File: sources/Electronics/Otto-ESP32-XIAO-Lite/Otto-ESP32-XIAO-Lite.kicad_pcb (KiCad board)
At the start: 2 copper layers, 60 x 52 mm, 54 parts, among them J1 Conn_01x03, J10 Conn_01x02, J12 OLED 0,91" - I2C (SKU21796), J13 MPU6050, J2 Conn_01x03, J3 Conn_01x03, J4 Conn_01x03, J5 Conn_01x03, J6 Conn_01x03, J7 Conn_01x04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

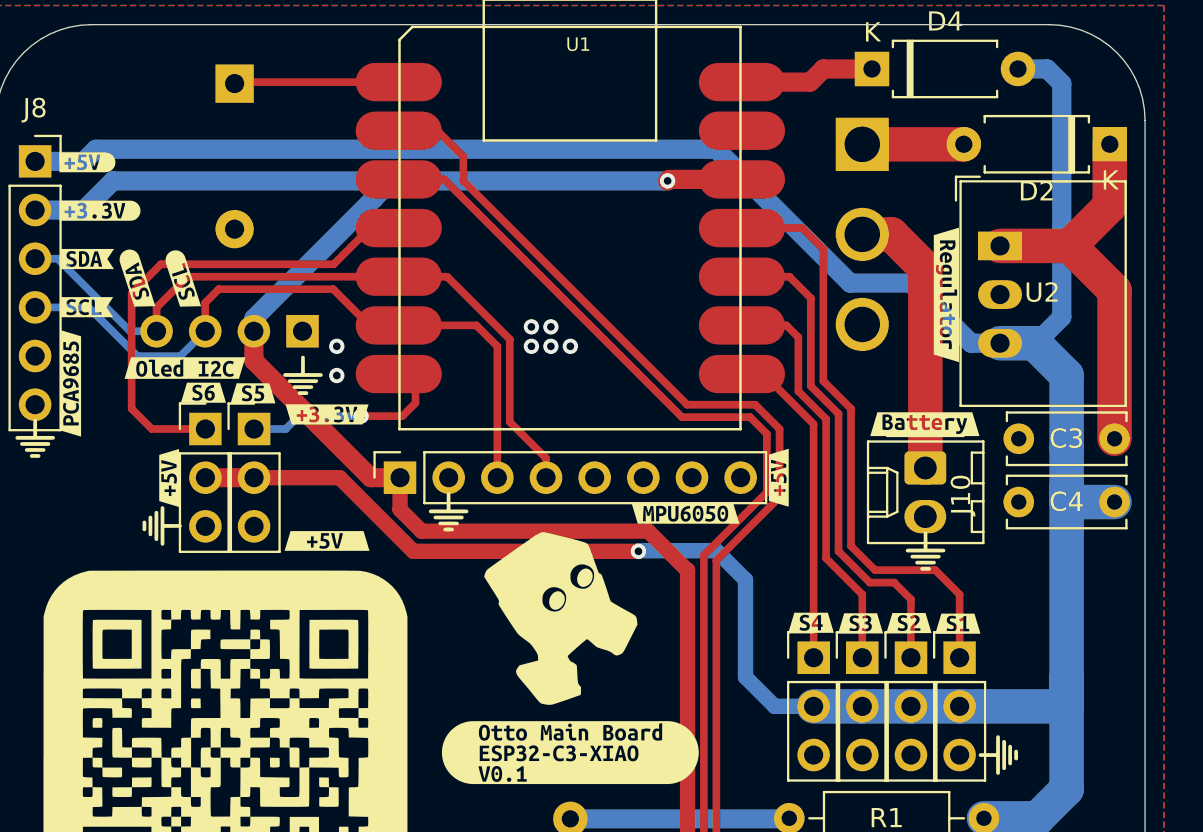
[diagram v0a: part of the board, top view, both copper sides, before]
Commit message: New version
- Add pinout servo documentation
- Remove diode D2
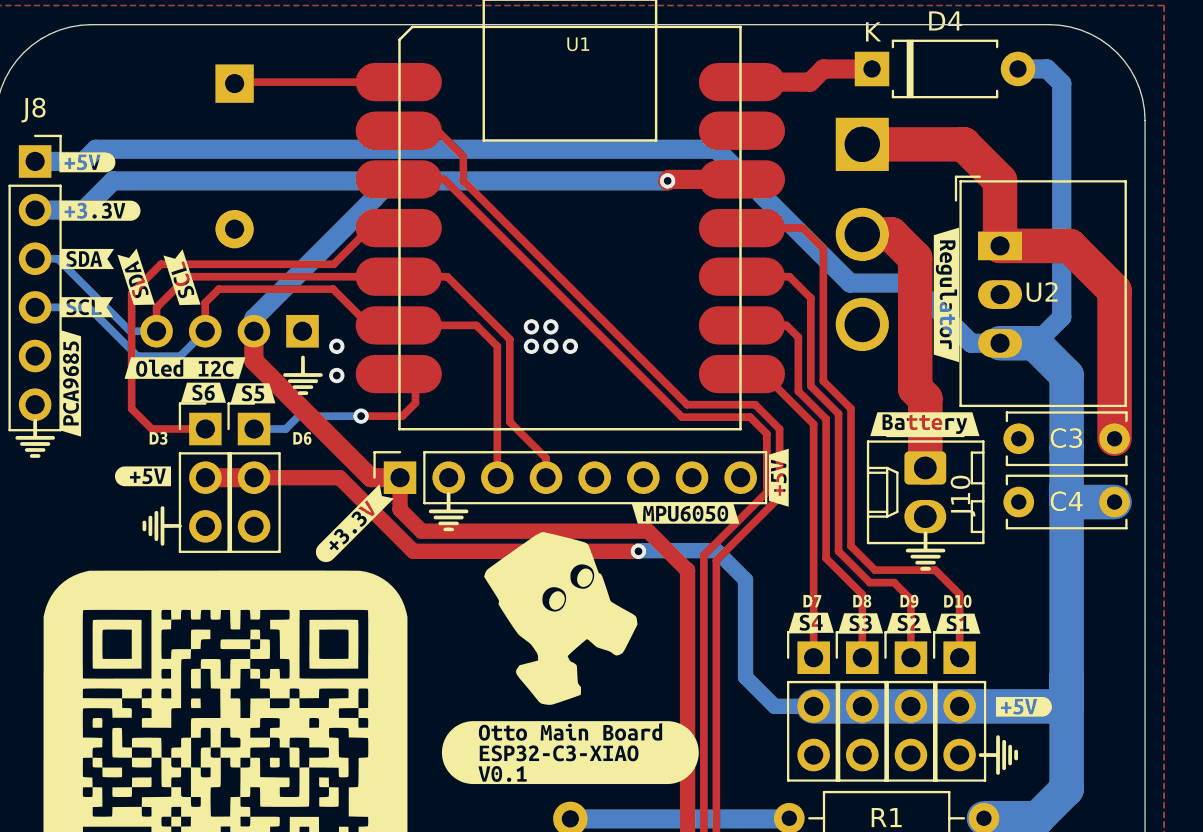
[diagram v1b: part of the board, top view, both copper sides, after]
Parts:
- removed D2: D_Small, Diode_THT:D_A-405_P7.62mm_Horizontal
- removed kibuzzard-66E45A06: G***, kibuzzard-66E45A06
- removed kibuzzard-66E45A30: G***, kibuzzard-66E45A30
- removed the kibuzzard-66E45B15 at (109.1, 73.7)
- removed kibuzzard-66E45B34: G***, kibuzzard-66E45B34
- removed kibuzzard-66E45C62: G***, kibuzzard-66E45C62
- removed kibuzzard-66E45C9B: G***, kibuzzard-66E45C9B
- added kibuzzard-66E45BAB: G***, kibuzzard-66E45BAB, F.Cu at (153.7, 85.6)
- added kibuzzard-676543B8: G***, kibuzzard-676543B8, F.Cu at (142.6, 81.2)
- added kibuzzard-6765451E: G***, kibuzzard-6765451E, F.Cu at (107.3, 63.3)
- added kibuzzard-67654523: G***, kibuzzard-67654523, F.Cu at (109.7, 63.3)
- added kibuzzard-6765454D: G***, kibuzzard-6765454D, F.Cu at (107.7, 73.6)
- added kibuzzard-67654588: G***, kibuzzard-67654588, F.Cu at (118.6, 76.1)
- J7: value Conn_01x04 -> Ultrasonic sensor
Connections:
- net EN-Driver renamed Servo-6
- SW1 pad 1: Net-(D2-A) -> +BATT
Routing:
- net Net-(D2-A): track 5.30 -> 0.00 mm
- net +BATT: track 20.8 -> 26.1 mm
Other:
- board text added: "D10"
- board text added: "D3"
- board text added: "D6"
- board text added: "D7"
- board text added: "D8"
- board text added: "D9"

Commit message: update documentation
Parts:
- moved kibuzzard-66E45B15 59.7 mm to (84.3, 92.7)
- moved kibuzzard-6707C6B3 59.7 mm to (93.1, 83.1)
- moved D1 59.7 mm to (73.4, 113.0)
- moved G*** 59.7 mm to (95.8, 107.1)
- moved G*** 59.7 mm to (67.1, 94.5)
- moved G*** 59.7 mm to (79.3, 117.0)
- moved J6 59.7 mm to (54.4, 90.1)
- moved J7 59.7 mm to (77.2, 119.0)
- moved J8 59.7 mm to (45.5, 76.2)
- moved kibuzzard-66E45B51 59.7 mm to (93.7, 100.3)
- moved kibuzzard-66E45BAB 59.7 mm to (48.2, 76.2)
- moved kibuzzard-6707CF99 59.7 mm to (73.4, 107.0)
- moved kibuzzard-67654523 59.7 mm to (53.2, 82.3)
- moved G*** 59.7 mm to (55.4, 107.0)
- moved J12 59.7 mm to (59.4, 85.0)
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
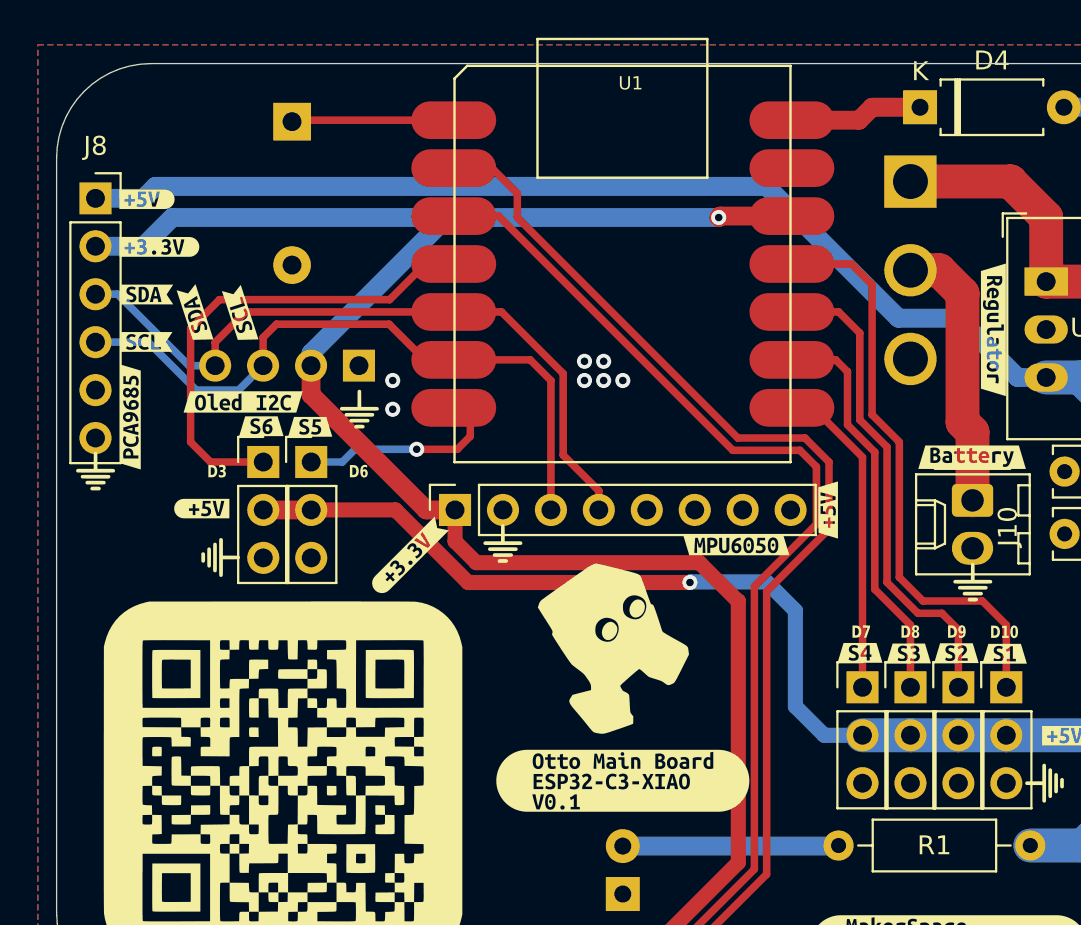
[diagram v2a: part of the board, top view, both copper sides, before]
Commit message: add header pin option for XIAO
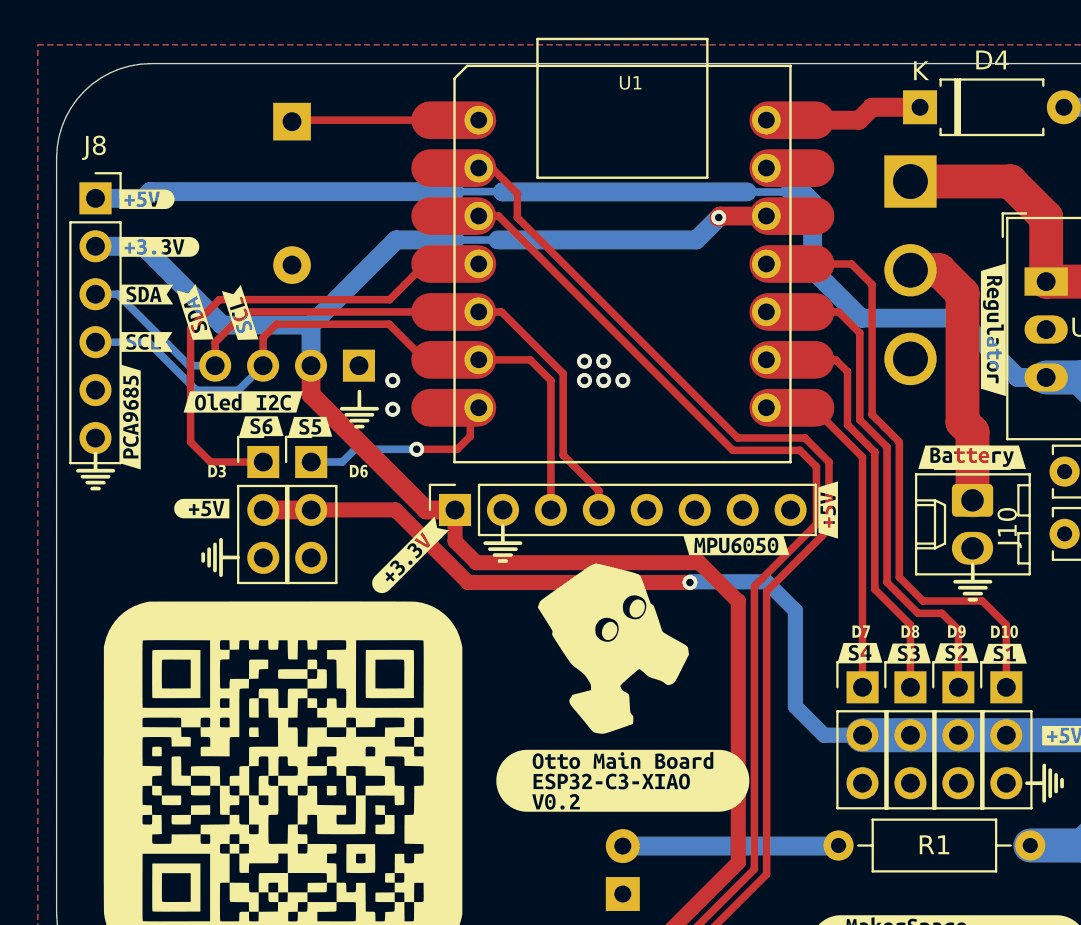
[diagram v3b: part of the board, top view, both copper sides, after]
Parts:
- removed kibuzzard-6707CF99: G***, kibuzzard-6707CF99
- added kibuzzard-69711E0F: G***, kibuzzard-69711E0F, F.Cu at (73.4, 107.0)
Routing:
- net +3.3V: track 104.2 -> 99.0 mm
- net +5V: track 161.8 -> 163.8 mm
